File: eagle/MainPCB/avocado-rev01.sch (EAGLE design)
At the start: 7 parts, among them U1 V3S

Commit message: updated schematic
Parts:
- added J1: 10118194-0001LF, 10118194-0001LF:10118194-0001LF
- added J2: CON-DSUB-15-VGA, m-pad-2.1:CON-DSUB-15-VGA
- added J3: 0475710001, 0475710001:0475710001
- X1: device marius:XTAL11.4X4.7 -> marius:XTAL3.2X2
- X2: device marius:XTALABS25 -> marius:XTAL5X1.9
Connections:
- new net N$6: J1.DP, U1G$5.USB-DP
- new net USB-ID: J1.ID
- new net VCC: J1.VCC
- net GND: now also J1.GND, J1.SHIELD
- net N$5: now also J1.DM, U1G$5.USB-DM; no longer U1G$6.AGND
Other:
- moved on the sheet: C1, C2, C3, C4, X1, X2

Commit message: updated schematic
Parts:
- added D1: LL-R3528RGBC-008-B, LL-R3528RGBC-008-B:LL-R3528RGBC-008-B
- added R1, R2, R3: (no value), resistor:R-EU_R0603
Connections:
- new net N$10: D1.CATHODE_RED, R3.2
- new net N$11: D1.CATHODE_GREEN, R2.1
- new net N$7: R1.2, U1G$5.EPHY_LINK_LED
- new net N$8: R2.2, U1G$5.EPHY_SPD_LED
- new net N$9: D1.CATHODE_BLUE, R1.1
- net GND: now also R3.1
- net VCC: now also D1.COMM_ANODE
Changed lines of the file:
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@@
 <part name="J2" library="m-pad-2.1" deviceset="CON-DSUB-15-VGA" device=""/>
 <part name="J3" library="0475710001" deviceset="0475710001" device=""/>
+<part name="D1" library="LL-R3528RGBC-008-B" deviceset="LL-R3528RGBC-008-B" device=""/>
+<part name="GND6" library="marius" library_urn="urn:adsk.eagle:library:5910807" deviceset="GND" device=""/>
+<part name="VCC1" library="m-pad-2.1" deviceset="VCC" device=""/>
+<part name="VCC2" library="m-pad-2.1" deviceset="VCC" device=""/>
+<part name="R1" library="resistor" library_urn="urn:adsk.eagle:library:348" deviceset="R-EU_" device="R0603" package3d_urn="urn:adsk.eagle:package:26057/1"/>
+<part name="R2" library="resistor" library_urn="urn:adsk.eagle:library:348" deviceset="R-EU_" device="R0603" package3d_urn="urn:adsk.eagle:package:26057/1"/>
+<part name="R3" library="resistor" library_urn="urn:adsk.eagle:library:348" deviceset="R-EU_" device="R0603" package3d_urn="urn:adsk.eagle:package:26057/1"/>
 </parts>
 <sheets>
@@
 <attribute name="VALUE" x="180.3387" y="66.0384" size="1.270159375" layer="96"/>
 </instance>
+<instance part="D1" gate="G$1" x="33.02" y="48.26" smashed="yes" rot="R90">
+<attribute name="NAME" x="17.7841" y="35.5162" size="1.78413125" layer="95" rot="R90"/>
+</instance>
+<instance part="GND6" gate="1" x="43.18" y="22.86" smashed="yes">
+<attribute name="VALUE" x="40.64" y="20.32" size="1.778" layer="96"/>
+</instance>
+<instance part="VCC1" gate="1" x="15.24" y="48.26" smashed="yes" rot="R90">
+<attribute name="VALUE" x="11.938" y="46.101" size="1.778" layer="96" rot="R90"/>
+</instance>
+<instance part="VCC2" gate="1" x="30.48" y="101.6" smashed="yes">
+<attribute name="VALUE" x="28.321" y="104.902" size="1.778" layer="96"/>
+</instance>
+<instance part="R1" gate="G$1" x="38.1" y="66.04" smashed="yes" rot="R90">
+<attribute name="NAME" x="36.6014" y="62.23" size="1.778" layer="95" rot="R90"/>
+<attribute name="VALUE" x="41.402" y="62.23" size="1.778" layer="96" rot="R90"/>
+</instance>
+<instance part="R2" gate="G$1" x="43.18" y="55.88" smashed="yes" rot="R90">
+<attribute name="NAME" x="41.6814" y="52.07" size="1.778" layer="95" rot="R90"/>
+<attribute name="VALUE" x="46.482" y="52.07" size="1.778" layer="96" rot="R90"/>
+</instance>
+<instance part="R3" gate="G$1" x="43.18" y="33.02" smashed="yes" rot="R90">
+<attribute name="NAME" x="41.6814" y="29.21" size="1.778" layer="95" rot="R90"/>
+<attribute name="VALUE" x="46.482" y="29.21" size="1.778" layer="96" rot="R90"/>
+</instance>
 </instances>
 <busses>
@@
 <wire x1="27.94" y1="83.82" x2="27.94" y2="76.2" width="0.1524" layer="91"/>
 <junction x="27.94" y="83.82"/>
+</segment>
+<segment>
+<pinref part="GND6" gate="1" pin="GND"/>
+<pinref part="R3" gate="G$1" pin="1"/>
+<wire x1="43.18" y1="25.4" x2="43.18" y2="27.94" width="0.1524" layer="91"/>
 </segment>
 </net>
@@
 <wire x1="27.94" y1="99.06" x2="30.48" y2="99.06" width="0.1524" layer="91"/>
 <wire x1="30.48" y1="99.06" x2="30.48" y2="101.6" width="0.1524" layer="91"/>
-<label x="30.48" y="101.6" size="1.778" layer="95"/>
+<pinref part="VCC2" gate="1" pin="VCC"/>
+</segment>
+<segment>
+<pinref part="D1" gate="G$1" pin="COMM_ANODE"/>
+<wire x1="20.32" y1="48.26" x2="15.24" y2="48.26" width="0.1524" layer="91"/>
+<pinref part="VCC1" gate="1" pin="VCC"/>
 </segment>
 </net>
@@
 </segment>
 </net>
+<net name="N$7" class="0">
+<segment>
+<pinref part="U1" gate="G$5" pin="EPHY_LINK_LED"/>
+<wire x1="53.34" y1="83.82" x2="38.1" y2="83.82" width="0.1524" layer="91"/>
+<pinref part="R1" gate="G$1" pin="2"/>
+<wire x1="38.1" y1="83.82" x2="38.1" y2="71.12" width="0.1524" layer="91"/>
+</segment>
+</net>
+<net name="N$8" class="0">
+<segment>
+<pinref part="U1" gate="G$5" pin="EPHY_SPD_LED"/>
+<wire x1="43.18" y1="76.2" x2="53.34" y2="76.2" width="0.1524" layer="91"/>
+<pinref part="R2" gate="G$1" pin="2"/>
+<wire x1="43.18" y1="60.96" x2="43.18" y2="76.2" width="0.1524" layer="91"/>
+</segment>
+</net>
+<net name="N$10" class="0">
+<segment>
+<pinref part="D1" gate="G$1" pin="CATHODE_RED"/>
+<wire x1="38.1" y1="38.1" x2="43.18" y2="38.1" width="0.1524" layer="91"/>
+<pinref part="R3" gate="G$1" pin="2"/>
+</segment>
+</net>
+<net name="N$11" class="0">
+<segment>
+<pinref part="D1" gate="G$1" pin="CATHODE_GREEN"/>
+<wire x1="38.1" y1="48.26" x2="43.18" y2="48.26" width="0.1524" layer="91"/>
+<pinref part="R2" gate="G$1" pin="1"/>
+<wire x1="43.18" y1="50.8" x2="43.18" y2="48.26" width="0.1524" layer="91"/>
+</segment>
+</net>
+<net name="N$9" class="0">
+<segment>
+<pinref part="R1" gate="G$1" pin="1"/>
+<pinref part="D1" gate="G$1" pin="CATHODE_BLUE"/>
+<wire x1="38.1" y1="60.96" x2="38.1" y2="58.42" width="0.1524" layer="91"/>
+</segment>
+</net>

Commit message: Connected power
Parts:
- added C10, C15, C5: 1u, marius:C0603
- added C11, C14, C16, C19, C6, C9: 100n, marius:C0603
- added C12, C13, C17, C18, C7, C8: 22u, marius:C_POL4.3
- added FID1, FID2: FIDUCIAL, marius:FIDUCIAL
- added L1, L2, L3: CALC, marius:L6X6
- added P2: CONNECTOR-15686115148922, marius:CONNECTOR-15686115148922
- added P3: PADTH, marius:PADTH
- added R10, R11, R14, R15, R6, R7: CALC, marius:R0603
- added R12, R4, R8: 100k, marius:R0603
- added R13, R5, R9: 59k, marius:R0603
- added R16: 0, marius:R0603
- added TP1: TEST_TESTPOINT, marius:TEST_TESTPOINT
- added U2, U3, U4: AP65111A, marius:AP65111A
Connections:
- new net 1V2: C18.+, C19.1, L3.2, R14.1, U1G$6.EPHY_VDD, U1G$6.VDD-CPU0, U1G$6.VDD-CPU1, U1G$6.VDD-CPU2, U1G$6.VDD-CPU3, U1G$6.VDD-CPU4, U1G$6.VDD-CPU5, U1G$6.VDD-CPU6, U1G$6.VDD-CPU7, U1G$6.VDD-SYS0, U1G$6.VDD-SYS1, U1G$6.VDD-SYS2, U1G$6.VDD-SYS3, U1G$6.VDD-SYS4, U1G$6.VDD-SYS5
- new net 1V8: C13.+, C14.1, L2.2, R10.1, U1G$7.VCC-DRAM0, U1G$7.VCC-DRAM1, U1G$7.VCC-DRAM10, U1G$7.VCC-DRAM11, U1G$7.VCC-DRAM2, U1G$7.VCC-DRAM3, U1G$7.VCC-DRAM4, U1G$7.VCC-DRAM5, U1G$7.VCC-DRAM6, U1G$7.VCC-DRAM7, U1G$7.VCC-DRAM8, U1G$7.VCC-DRAM9
- new net 3V: U1G$6.AVCC, U1G$6.VCC-PLL
- new net 3V3: C8.+, C9.1, L1.2, R16.2, R6.1, U1G$6.EPHY_VCC, U1G$6.VCC-0, U1G$6.VCC-1, U1G$6.VCC-2, U1G$6.VCC-3, U1G$6.VCC-MCSI, U1G$6.VCC-PE0, U1G$6.VCC-PE1, U1G$6.VCC-USB
- new net N$13: R16.1, U1G$6.VCC-RTC
- new net N$15: R5.2, U2.FB
- new net N$16: C5.2, L1.1, U2.SW
- new net N$17: R5.1, R6.2, R7.1
- new net N$18: C5.1, U2.BST
- new net N$19: R4.1, U2.ENABLE
- new net N$20: R9.2, U3.FB
- new net N$21: C10.2, L2.1, U3.SW
- new net N$22: R10.2, R11.1, R9.1
- new net N$23: C10.1, U3.BST
- new net N$25: R8.1, U3.ENABLE
- new net N$27: R13.2, U4.FB
- new net N$28: C15.2, L3.1, U4.SW
- new net N$29: R13.1, R14.2, R15.1
- new net N$30: C15.1, U4.BST
- new net N$31: R12.1, U4.ENABLE
- new net N$34: U1G$6.RTC-VIO
- new net N$42: U1G$7.SZQ
- new net N$43: U1G$7.SVREF0
- new net N$44: U1G$7.SVREF1
- new net VIN: C11.1, C12.+, C16.1, C17.+, C6.1, C7.+, R12.2, R4.2, R8.2, U2.VIN, U3.VIN, U4.VIN
- net GND: now also C11.2, C12.-, C13.-, C14.2, C16.2, C17.-, C18.-, C19.2, C6.2, C7.-, C8.-, C9.2, R11.2, R15.2, R7.2, U1G$6.AGND, U1G$6.PAD, U2.GND, U3.GND, U4.GND

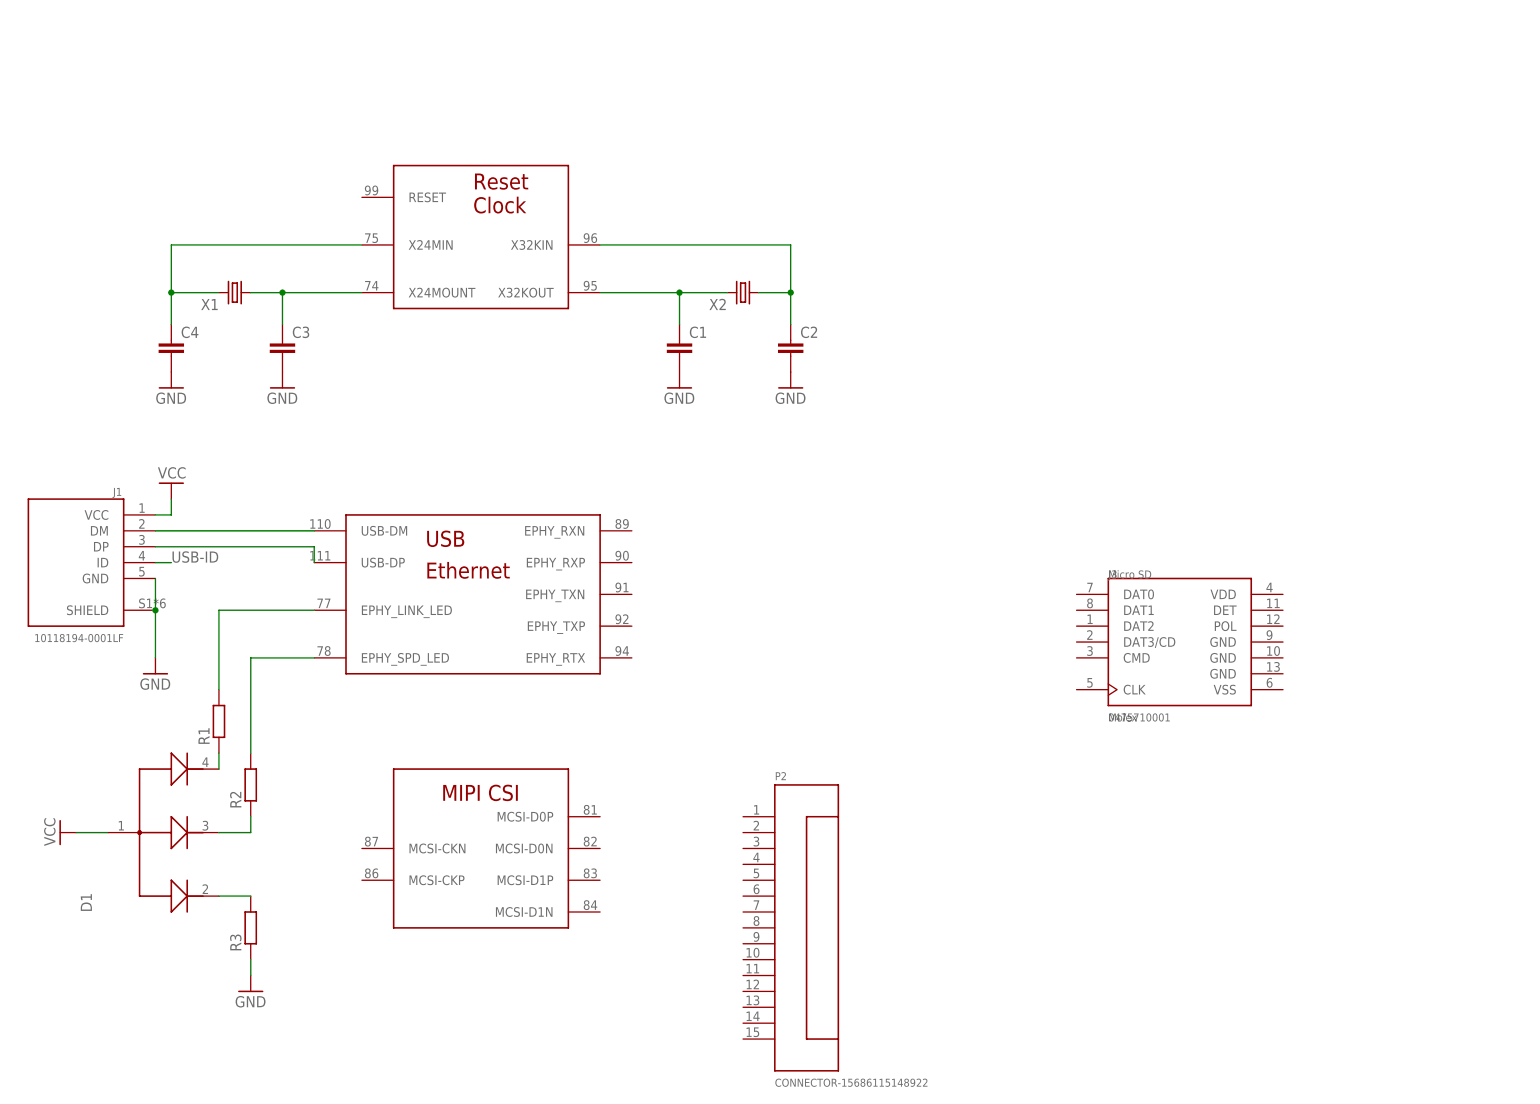
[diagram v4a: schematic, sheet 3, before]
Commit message: connected sd card and added led
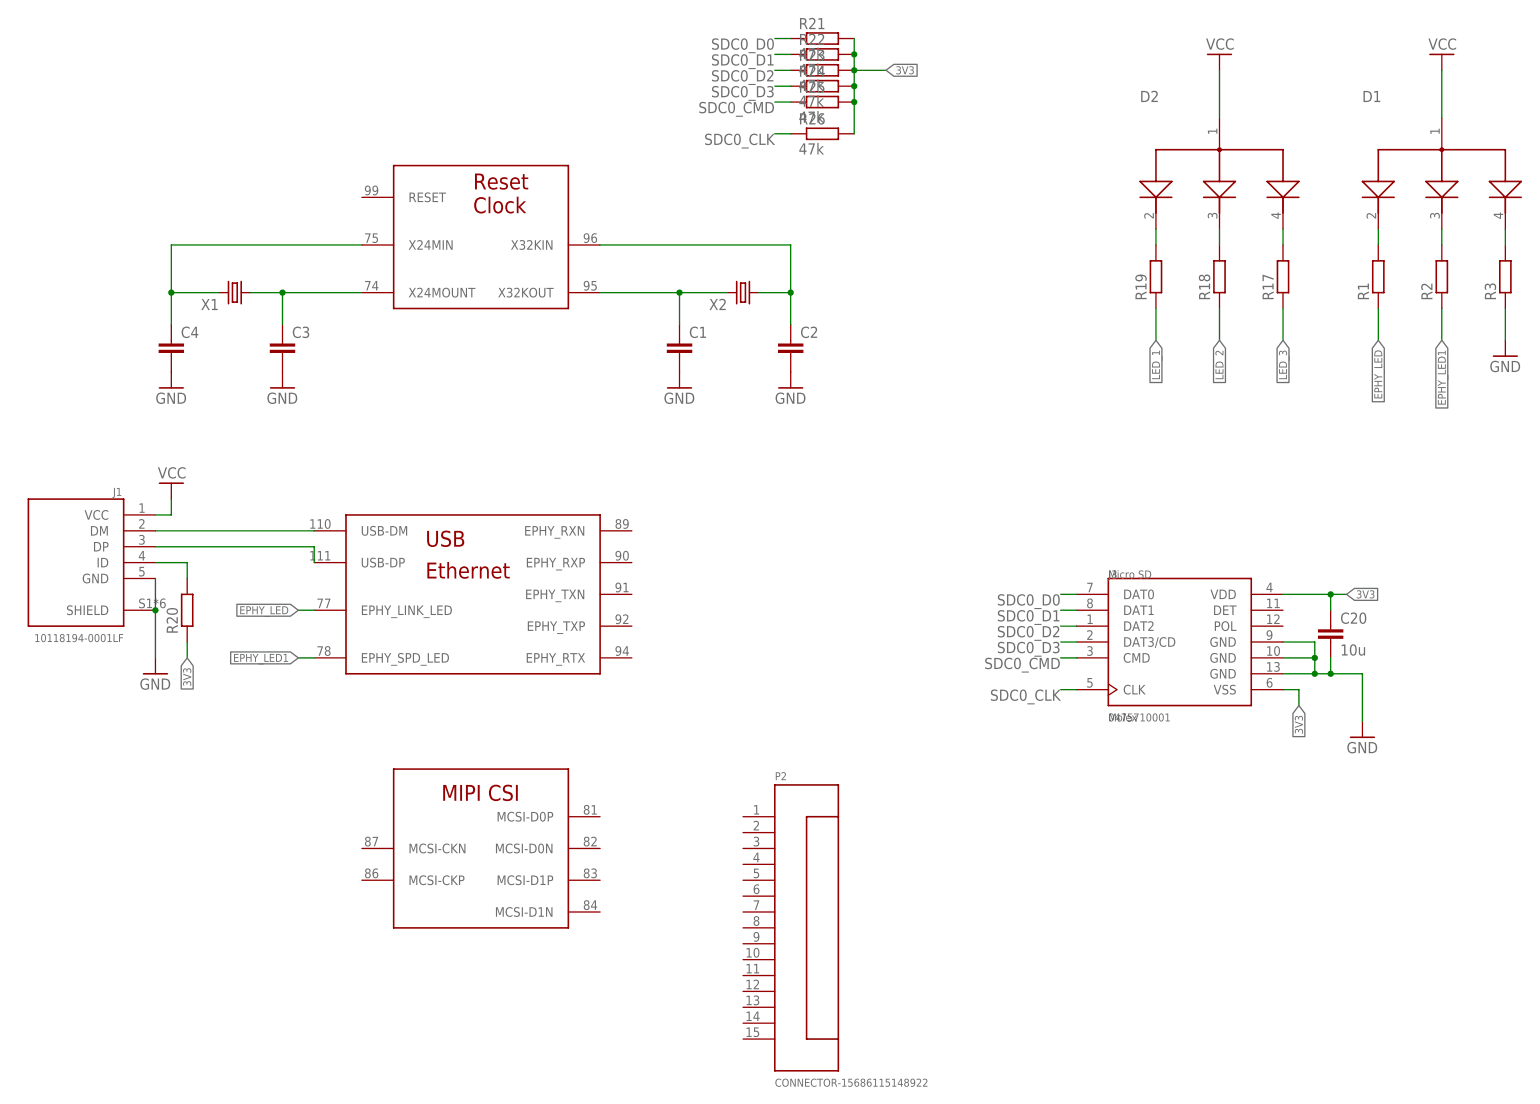
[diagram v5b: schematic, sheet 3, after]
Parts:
- added C20: 10u, marius:C0603
- added D2: LL-R3528RGBC-008-B, LL-R3528RGBC-008-B:LL-R3528RGBC-008-B
- added R17, R18, R19, R20: (no value), resistor:R-EU_R0603
- added R21, R22, R23, R24, R25, R26: 47k, resistor:R-EU_R0603
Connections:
- new net N$12: D1.CATHODE_RED, R1.2
- new net N$14: D1.CATHODE_GREEN, R2.2
- new net N$24: D1.CATHODE_BLUE, R3.2
- new net N$26: R2.1
- new net N$32: R1.1
- new net N$33: R17.1
- new net N$35: R18.1
- new net N$36: R19.1
- new net N$37: U1G$2.PG0/SDC1/CLK
- new net N$38: U1G$2.PG1/SDC1/CMD
- new net N$39: U1G$2.PG2/SDC1/D0
- new net N$40: R20.1
- new net N$41: R21.2, R22.2, R23.2, R24.2, R25.2, R26.2
- new net N$45: C20.1, J3.VDD
- new net N$46: J3.VSS
- new net SDC0_CLK: J3.CLK, R26.1, U1G$2.PF2/SDC0/CLK
- new net SDC0_CMD: J3.CMD, R25.1, U1G$2.PF3/SDC0/CMD
- new net SDC0_D0: J3.DAT0, R21.1, U1G$2.PF1/SDC0/D0
- new net SDC0_D1: J3.DAT1, R22.1, U1G$2.PF0/SDC0/D1
- new net SDC0_D2: J3.DAT2, R23.1, U1G$2.PF5/SDC0/D2
- new net SDC0_D3: J3.DAT3/CD, R24.1, U1G$2.PF4/SDC0/D3
- net GND: now also C20.2, J3.GND@1, J3.GND@2, J3.GND@3
- net N$10: now also D2.CATHODE_GREEN, R18.2; no longer D1.CATHODE_RED, R3.2
- net N$11: now also D2.CATHODE_BLUE, R17.2; no longer D1.CATHODE_GREEN, R2.1
- net N$7: no longer R1.2
- net N$8: no longer R2.2
- net N$9: now also D2.CATHODE_RED, R19.2; no longer D1.CATHODE_BLUE, R1.1
- net USB-ID: now also R20.2
- net VCC: now also D2.COMM_ANODE
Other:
- moved on the sheet: D1, R1, R2, R3
